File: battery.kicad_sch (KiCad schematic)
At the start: 41 parts, among them J15 Conn_01x02_Pin, J3 Lipo, Q2 AO3401A, Q3 IRLZ44N, Q4 IRLZ44N, Q5 2N7002, SW2 SW_Push, U2 BQ76920PW

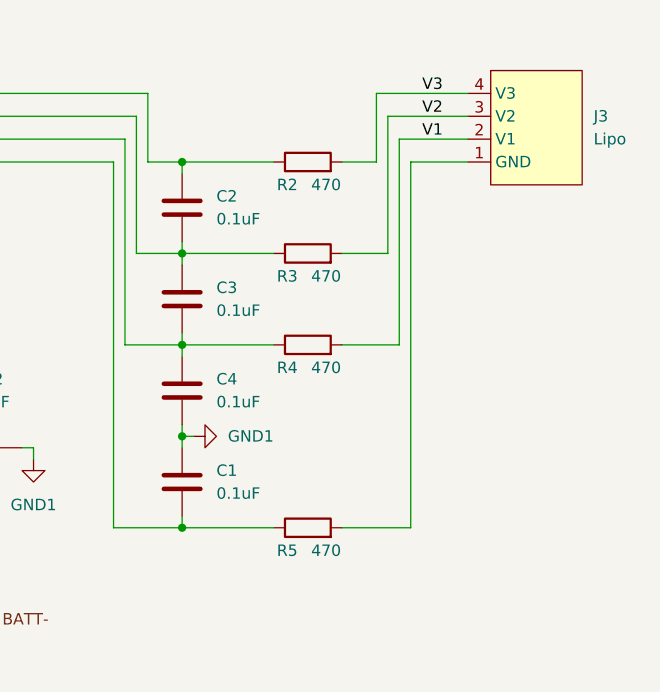
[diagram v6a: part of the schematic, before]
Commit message: cleaned up some traces
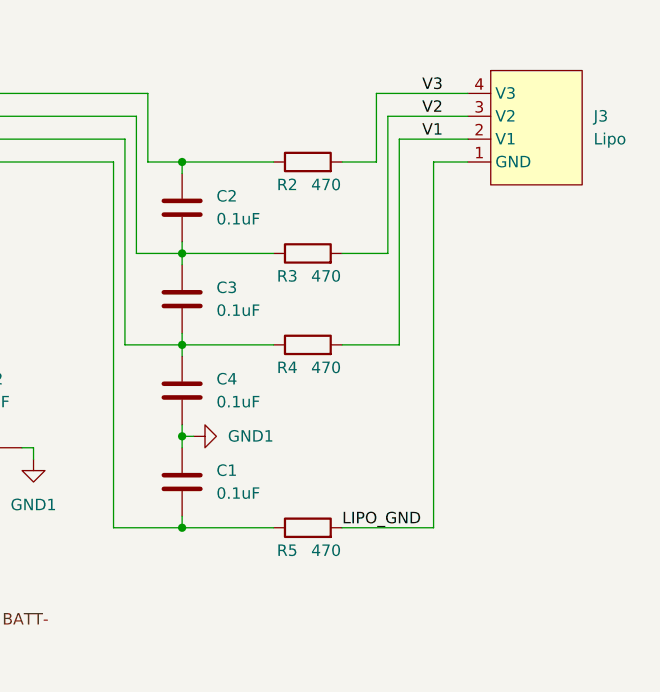
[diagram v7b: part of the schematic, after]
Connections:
- net LIPO_GND: now reaches J3.1 (GND), R5.2
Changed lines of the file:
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@@
 	(wire
 		(pts
-			(xy 259.08 92.71) (xy 259.08 133.35)
+			(xy 261.62 92.71) (xy 261.62 133.35)
 		)
 		(stroke
@@
 	(wire
 		(pts
-			(xy 251.46 133.35) (xy 259.08 133.35)
+			(xy 251.46 133.35) (xy 261.62 133.35)
 		)
 		(stroke
@@
 	(wire
 		(pts
-			(xy 265.43 92.71) (xy 259.08 92.71)
+			(xy 265.43 92.71) (xy 261.62 92.71)
 		)
 		(stroke
@@
 		(effects
 			(font
+				(size 1.27 1.27)
+			)
+			(justify left bottom)
+		)
+	)
+	(label "LIPO_GND"
+		(at 251.46 133.35 0)
+		(effects
+			(font

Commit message: added some lcsc part ids
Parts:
- F1: footprint Fuse:Fuse_2920_7451Metric -> Fuse:Fuse_Bourns_MF-RG900
- Q2: LCSC (none) -> C15127
- Q3, Q4: LCSC (none) -> C38774
- Q5: LCSC (none) -> C65189
- TH1: LCSC (none) -> C209959
- U2: LCSC (none) -> C601650
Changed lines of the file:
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@@
 			)
 		)
+		(property "LCSC" "C15127"
+			(at 149.86 121.92 90)
+			(effects
+				(font
+					(size 1.27 1.27)
+				)
+				(hide yes)
+			)
+		)
 		(pin "1"
 		)
@@
 			)
 		)
-		(property "LCSC" ""
+		(property "LCSC" "C601650"
 			(at 166.37 85.09 0)
 			(effects
@@
 			)
 		)
+		(property "LCSC" "C38774"
+			(at 135.89 140.97 90)
+			(effects
+				(font
+					(size 1.27 1.27)
+				)
+				(hide yes)
+			)
+		)
 		(pin "2"
 		)
@@
 			)
 		)
+		(property "LCSC" "C65189"
+			(at 128.27 115.57 90)
+			(effects
+				(font
+					(size 1.27 1.27)
+				)
+				(hide yes)
+			)
+		)
 		(pin "3"
 		)
@@
 			)
 		)
-		(property "LCSC" ""
+		(property "LCSC" "C209959"
 			(at 115.57 93.98 0)
 			(effects
@@
 			)
 		)
-		(property "Footprint" "Fuse:Fuse_2920_7451Metric"
+		(property "Footprint" "Fuse:Fuse_Bourns_MF-RG900"
 			(at 110.49 142.24 0)
 			(effects
@@
 			(effects
 				(font
+					(size 1.27 1.27)
+				)
+				(hide yes)
+			)
+		)
+		(property "LCSC" "C38774"
+			(at 160.02 140.97 90)
+			(effects
+				(font
